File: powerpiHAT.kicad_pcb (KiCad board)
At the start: 2 copper layers, 65 x 56.5 mm, 38 parts, among them J1 Conn_01x10, J2 AudioJack2_Dual_Ground_Switche, J3 40HAT, J4 AudioJack2_Dual_Ground_Switche, J5 AudioJack2_Dual_Ground_Switche, J6 AudioJack2_Dual_Ground_Switche, J7 Barrel_Jack, J8 Conn_01x04, Q1 DMG2305UX, Q2 DMMT5401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

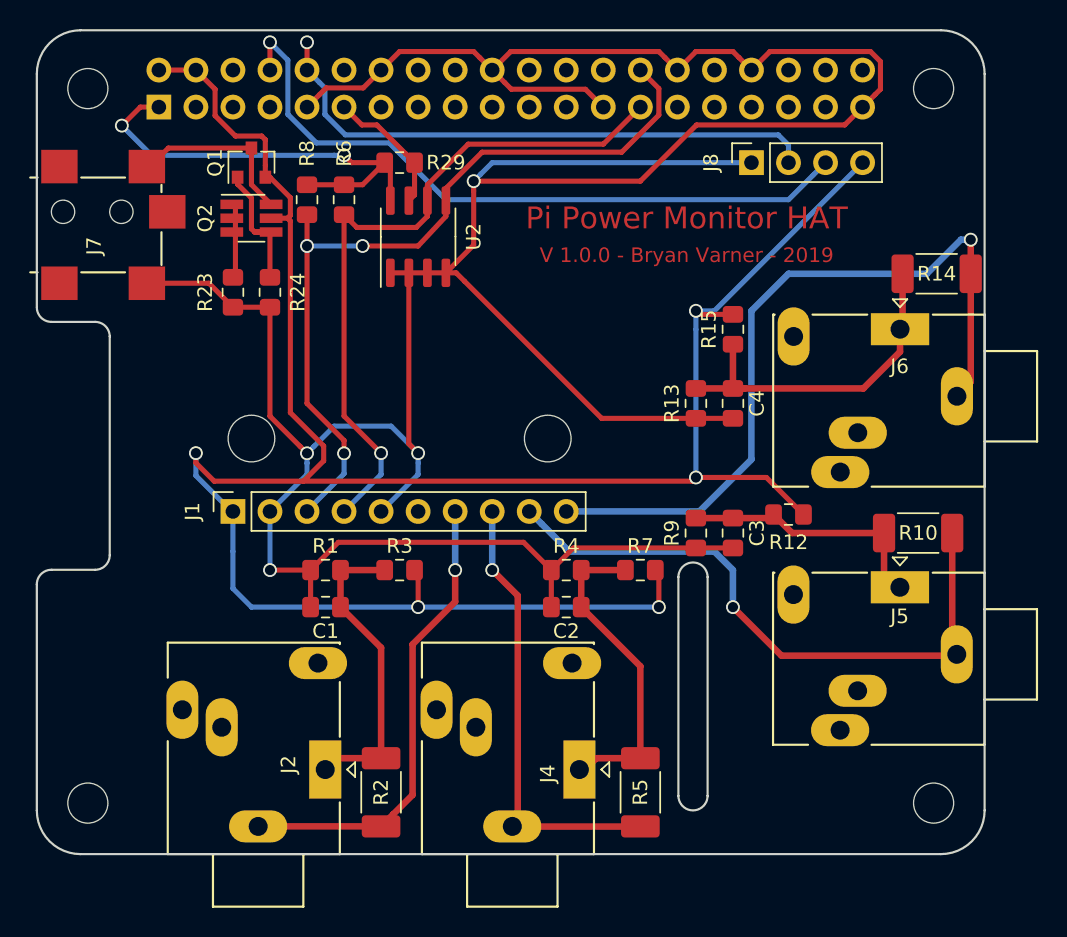
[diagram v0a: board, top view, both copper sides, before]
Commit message: Mounting holes are now through-hole, so we get reference points for drilling (drill marks) by hand.
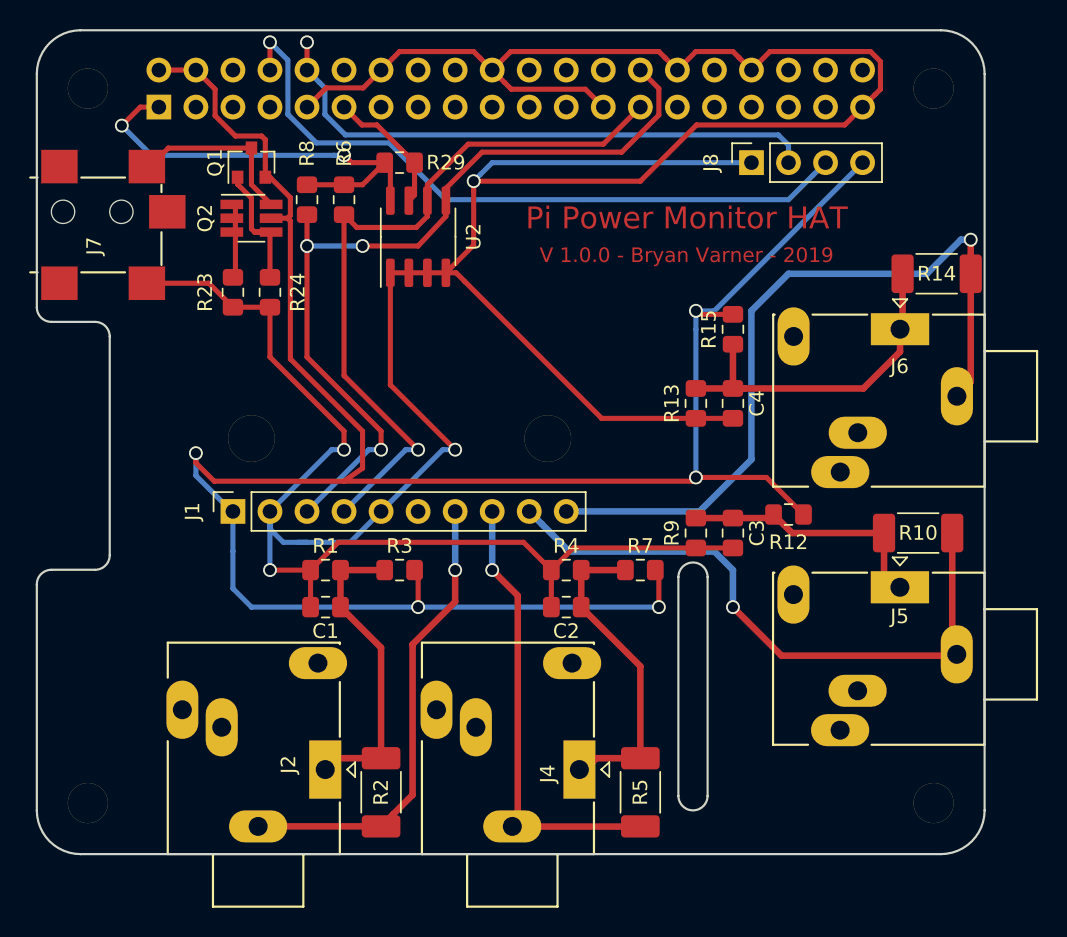
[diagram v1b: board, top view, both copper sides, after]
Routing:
- net GND: track 234.6 -> 241.9 mm
- net /ID_SD_EEPROM: track 47.8 -> 50.4 mm
- net /ID_SC_EEPROM: track 55.1 -> 57.7 mm
- net /P5V_HAT: track 156.6 -> 157.8 mm

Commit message: Moved the I2C For the ADS to the proper lines.
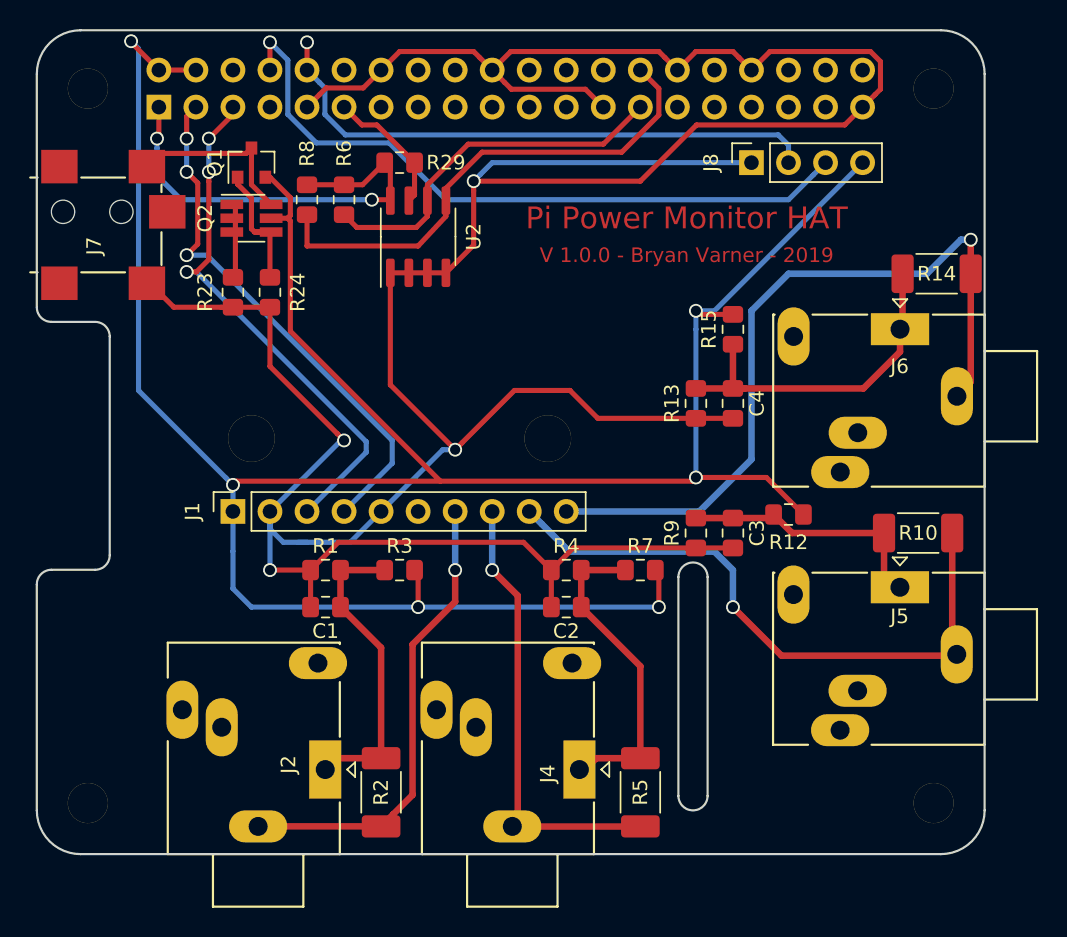
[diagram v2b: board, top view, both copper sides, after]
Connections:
- J1 pad 3: /ID_SC_EEPROM -> /BCM_3
- J1 pad 4: /ID_SD_EEPROM -> /BCM_2
- J3 pad 3: (no net) -> /BCM_2
- J3 pad 5: (no net) -> /BCM_3
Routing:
- net /BCM_2: track 0.00 -> 36.6 mm, vias 0 -> 3
- net /BCM_3: track 0.00 -> 36.6 mm, vias 0 -> 3
- net /ID_SD_EEPROM: track 50.4 -> 25.4 mm, vias 1 -> 0
- net /ID_SC_EEPROM: track 57.7 -> 34.8 mm, vias 3 -> 0
- net /P5V_HAT: track 157.8 -> 178.1 mm, vias 5 -> 6
- net GND: track 241.9 -> 239.2 mm
- net /P3V3_HAT: track 30.9 -> 30.2 mm

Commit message: Mount positions for the adafruit module. I happen to have both types on-hand for testing.d
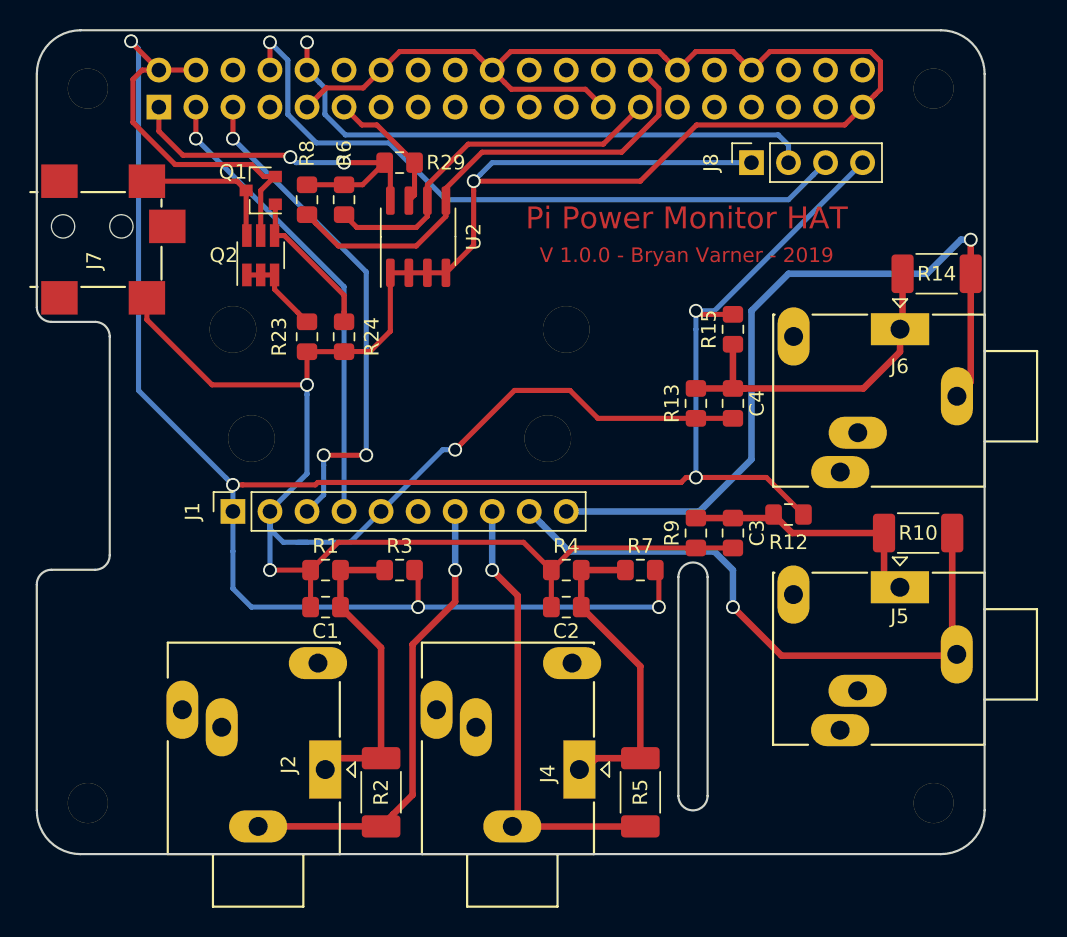
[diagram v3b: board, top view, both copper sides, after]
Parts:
- added H7: 3mm_Mounting_Hole, MountingHole:MountingHole_3.2mm_M3_DIN965, F.Cu at (111.5, 80.5)
- added H8: 3mm_Mounting_Hole, MountingHole:MountingHole_3.2mm_M3_DIN965, F.Cu at (134.3, 80.5)
- moved R23 5.92 mm to (116.5, 81.0)
- moved R24 5.92 mm to (119.1, 81.0)
- moved Q2 2.62 mm to (113.4, 75.4), turned to 90 degrees
- moved Q1 2.01 mm to (113.4, 71.0), turned to 180 degrees
- moved J7 1.00 mm to (97.3, 71.3)
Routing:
- net /P5V_HAT: track 178.1 -> 171.6 mm
- net /BCM_2: track 36.6 -> 31.9 mm, vias 3 -> 1
- net GND: track 239.2 -> 234.7 mm
- net /P3V3_HAT: track 30.2 -> 26.7 mm
- net /P5V: track 11.9 -> 10.2 mm
- net /BCM_3: track 36.6 -> 34.9 mm
- net /ID_SC_EEPROM: track 34.8 -> 33.5 mm
- net Net-(Q1-Pad1): track 9.43 -> 10.4 mm
- net Net-(Q2-Pad1): track 5.08 -> 6.03 mm
